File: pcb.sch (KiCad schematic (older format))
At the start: 5 parts, among them J0 USB_mini_micro_B, P1 CONN_3X2, P2 CONN_4

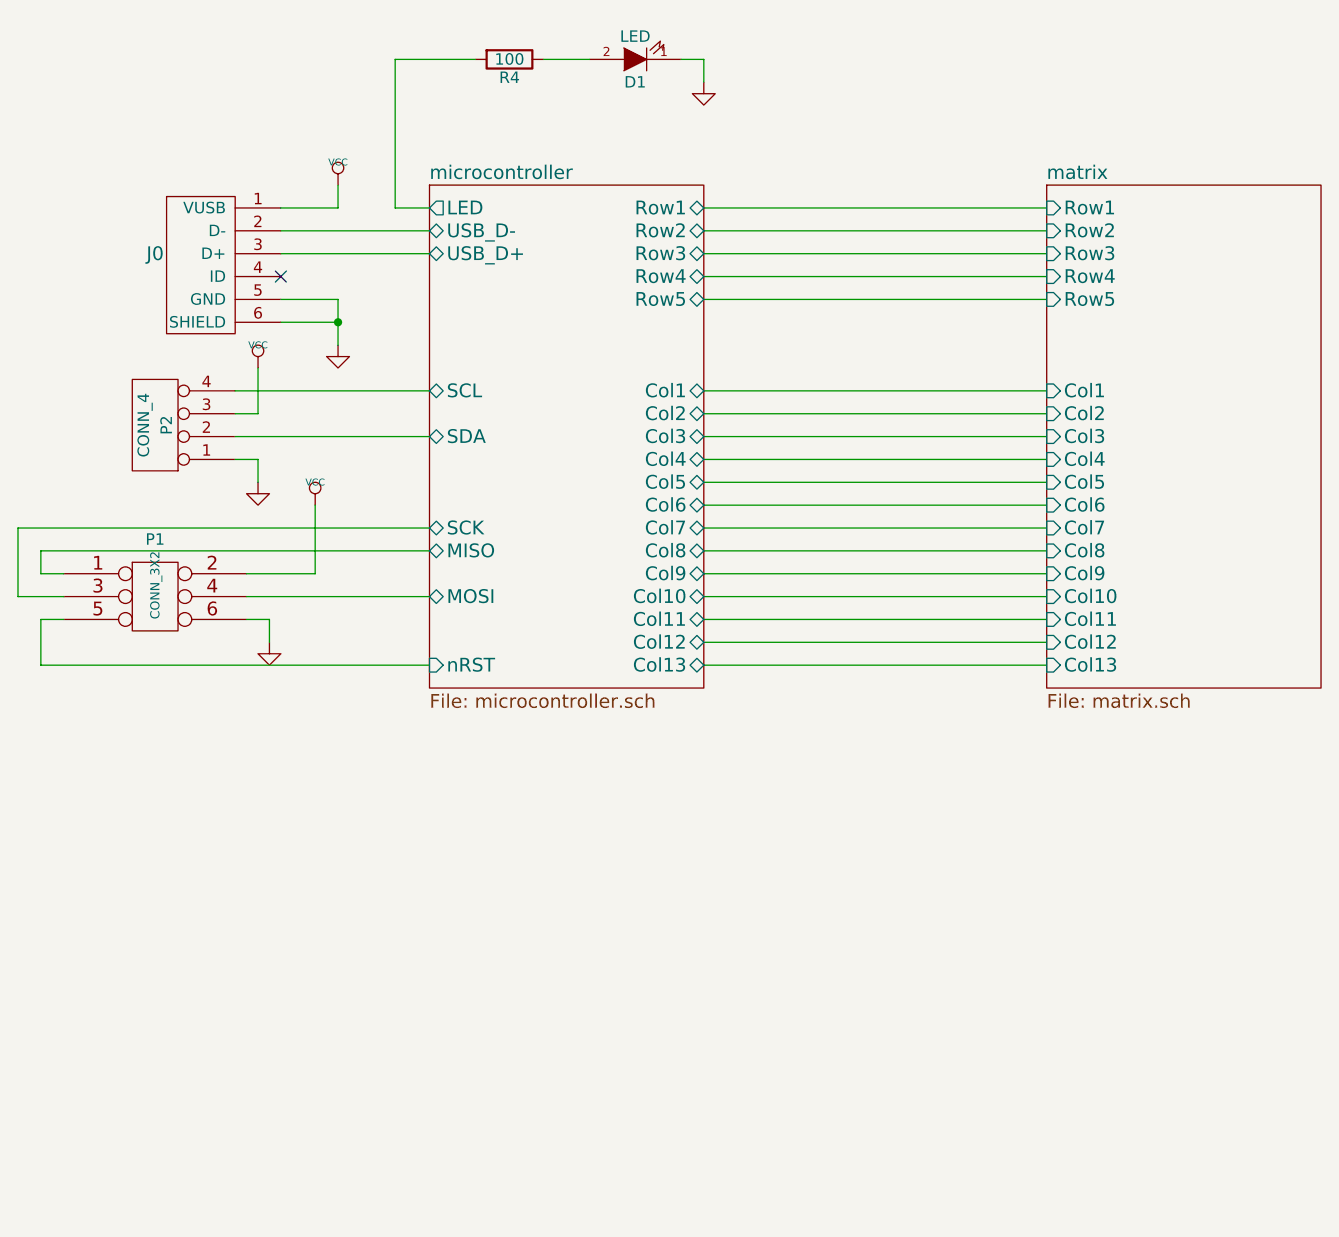
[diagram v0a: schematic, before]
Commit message: Branch for finalizing the board.
TODO:
Swap to smaller components, finalize pads
Added footprints.pretty
Add RGB underglow
Added schematic library (keenkeeb.lib/dcm)
Remove SPI header (?)
Add test pads (?)
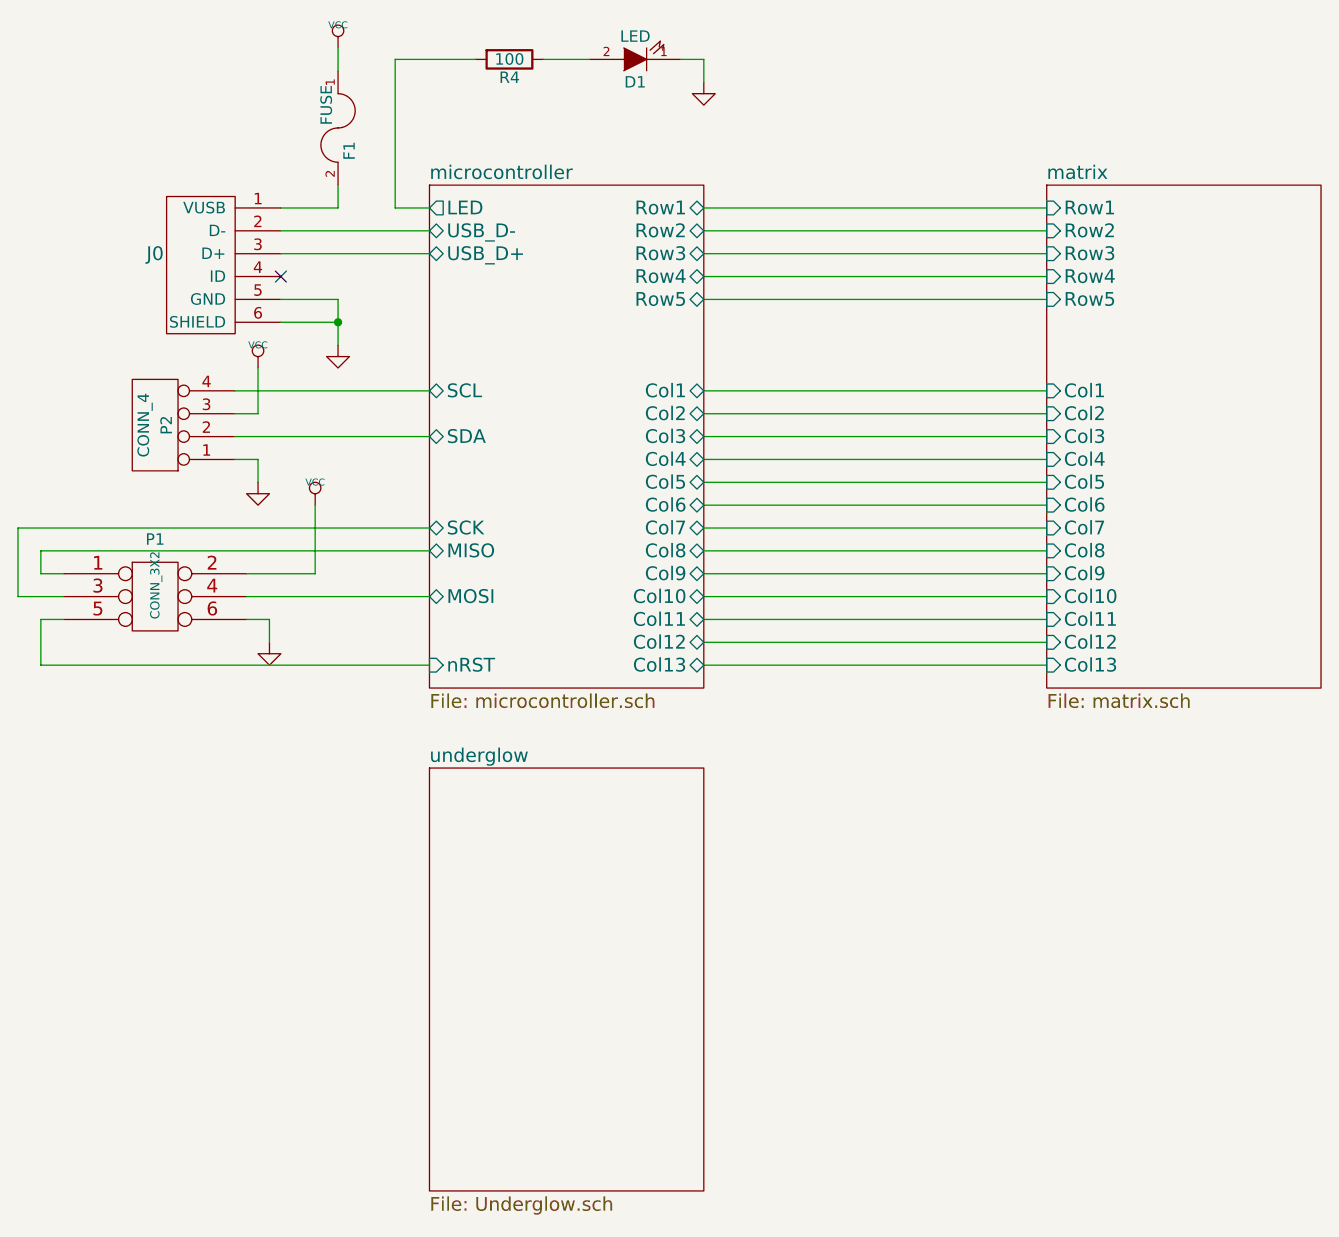
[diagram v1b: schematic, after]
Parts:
- added F1: FUSE, LEDs:LED_0805, symbol FUSE
- D1: footprint Keyboards:LED_3mm_plusminus -> footprints:LED_3mm_plusminus
- R4: footprint Resistors_SMD:R_0805_HandSoldering -> Resistors_SMD:R_0805
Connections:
- net VCC: now also F1.1; no longer J0.1 (VUSB)
- new net: F1.2, J0.1 (VUSB)
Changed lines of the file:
@@
 LIBS:contrib
 LIBS:valves
+LIBS:keenkeeb
 LIBS:keyboard_parts
 LIBS:pcb-cache
@@
 $Descr A4 11693 8268
 encoding utf-8
-Sheet 1 3
+Sheet 1 4
 Title ""
 Date ""
@@
 L VCC #PWR01
 U 1 1 587BC255
-P 3600 2250
-F 0 "#PWR01" H 3600 2350 30  0001 C CNN
-F 1 "VCC" H 3600 2350 30  0000 C CNN
-F 2 "" H 3600 2250 60  0001 C CNN
-F 3 "" H 3600 2250 60  0001 C CNN
-	1    3600 2250
+P 3600 1650
+F 0 "#PWR01" H 3600 1750 30  0001 C CNN
+F 1 "VCC" H 3600 1750 30  0000 C CNN
+F 2 "" H 3600 1650 60  0001 C CNN
+F 3 "" H 3600 1650 60  0001 C CNN
+	1    3600 1650
 	1    0    0    -1
 $EndComp
@@
 F 0 "D1" H 4900 1800 50  0000 C CNN
 F 1 "LED" H 4900 1600 50  0000 C CNN
-F 2 "Keyboards:LED_3mm_plusminus" H 4900 1700 60  0001 C CNN
+F 2 "footprints:LED_3mm_plusminus" H 4900 1700 60  0001 C CNN
 F 3 "" H 4900 1700 60  0001 C CNN
 	1    4900 1700
@@
 F 0 "R4" V 4430 1700 50  0000 C CNN
 F 1 "100" V 4350 1700 50  0000 C CNN
-F 2 "Resistors_SMD:R_0805_HandSoldering" H 4350 1700 60  0001 C CNN
+F 2 "Resistors_SMD:R_0805" H 4350 1700 60  0001 C CNN
 F 3 "" H 4350 1700 60  0001 C CNN
 	1    4350 1700
@@
 Wire Wire Line
 	5100 1700 5200 1700
+$Sheet
+S 4000 4800 1200 1850
+U 591558FE
+F0 "underglow" 60
+F1 "Underglow.sch" 60
+$EndSheet
+$Comp
+L FUSE F1
+U 1 1 5916B62D
+P 3600 2000
+F 0 "F1" H 3700 2050 50  0000 C CNN
+F 1 "FUSE" H 3500 1950 50  0000 C CNN
+F 2 "LEDs:LED_0805" H 3600 2000 50  0001 C CNN
+F 3 "" H 3600 2000 50  0000 C CNN
+	1    3600 2000
+	0    1    1    0
+$EndComp
+Wire Wire Line
+	3600 1650 3600 1750
 $EndSCHEMATC

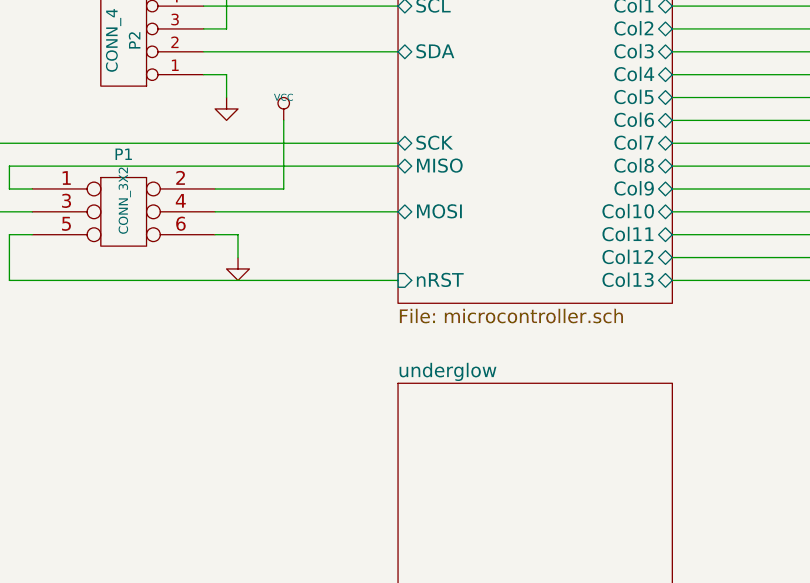
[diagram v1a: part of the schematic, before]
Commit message: ARR GEE BEE!!!
Added pads for WS2812B underglow - connected to pin 11.
Rerouted some connections.
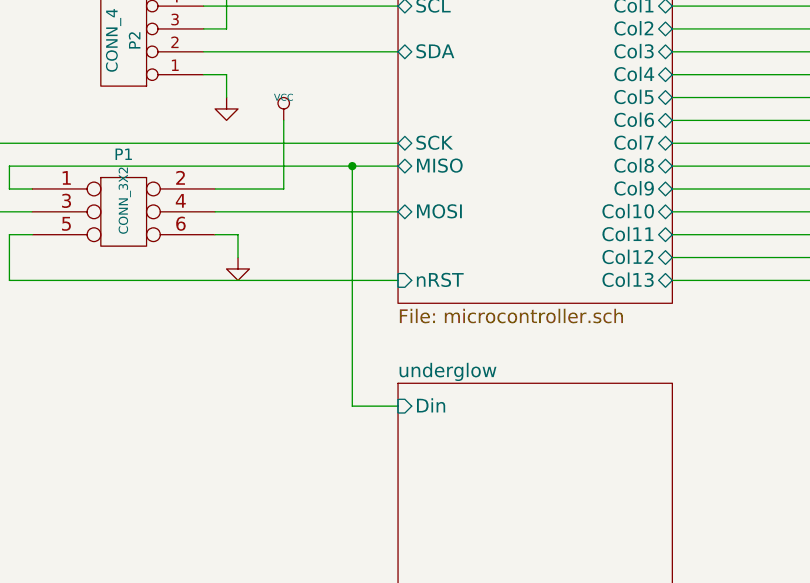
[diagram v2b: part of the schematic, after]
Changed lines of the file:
@@
 F0 "underglow" 60
 F1 "Underglow.sch" 60
+F2 "Din" I L 4000 4900 60
 $EndSheet
 $Comp
@@
 Wire Wire Line
 	3600 1650 3600 1750
+Wire Wire Line
+	4000 4900 3800 4900
+Wire Wire Line
+	3800 4900 3800 3850
+Connection ~ 3800 3850
 $EndSCHEMATC

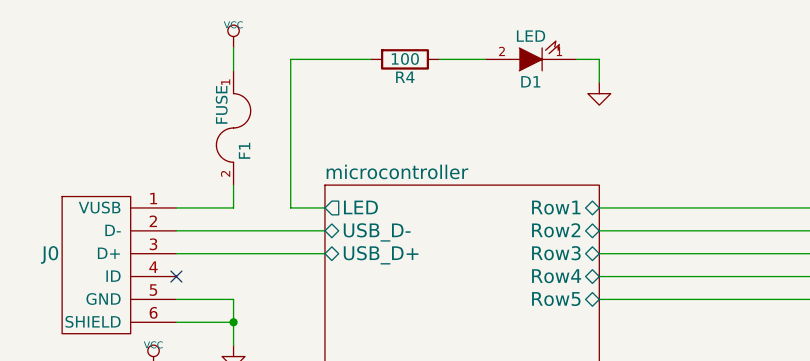
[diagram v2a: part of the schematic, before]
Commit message: Added 0.1uF caps to LEDs
Added capacitors from Vcc to GND for WS2812s
Also changed some references
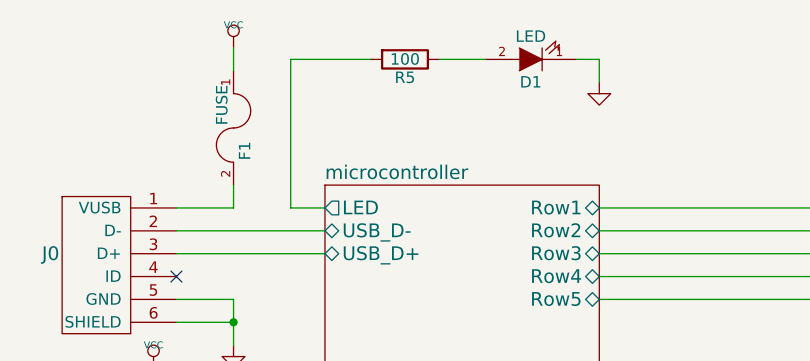
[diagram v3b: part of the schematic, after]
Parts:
- renumbered R4 to R5
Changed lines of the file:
@@
 $EndComp
 $Comp
-L R R4
+L R R5
 U 1 1 591032AE
 P 4350 1700
-F 0 "R4" V 4430 1700 50  0000 C CNN
+F 0 "R5" V 4430 1700 50  0000 C CNN
 F 1 "100" V 4350 1700 50  0000 C CNN
 F 2 "Resistors_SMD:R_0805" H 4350 1700 60  0001 C CNN

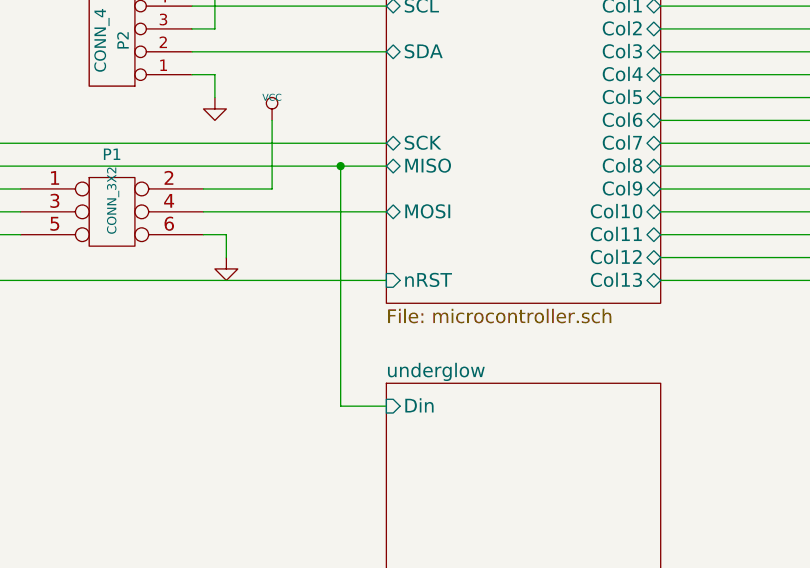
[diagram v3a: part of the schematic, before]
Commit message: Started to layout with MX/Alps footprints
Added footprints that support Cherry MX and Alps switches.
Started to layout the board with new footprints.  Will support PCB
mounted switches/stabs.
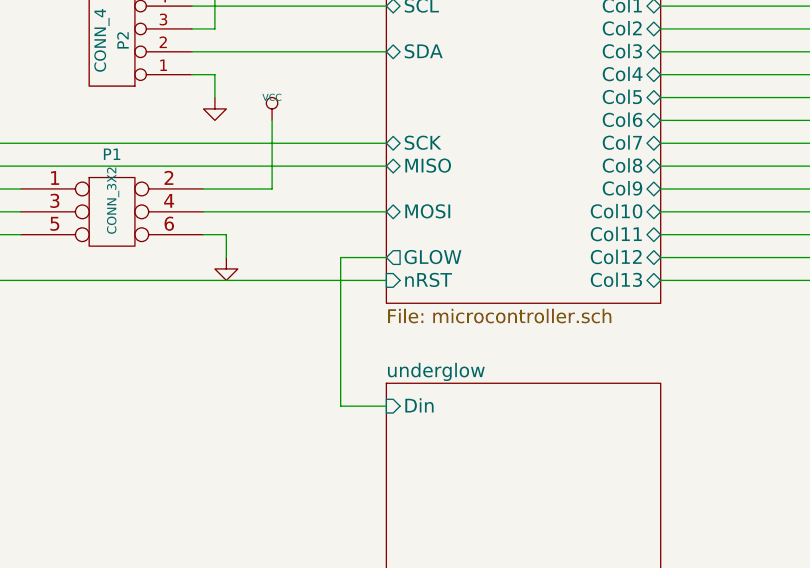
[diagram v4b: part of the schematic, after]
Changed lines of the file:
@@
 F27 "nRST" I L 4000 4350 60
 F28 "LED" O L 4000 2350 60
+F29 "GLOW" O L 4000 4250 60
 $EndSheet
 $Comp
@@
 	4000 4900 3800 4900
 Wire Wire Line
-	3800 4900 3800 3850
-Connection ~ 3800 3850
+	4000 4250 3800 4250
+Wire Wire Line
+	3800 4250 3800 4900
 $EndSCHEMATC

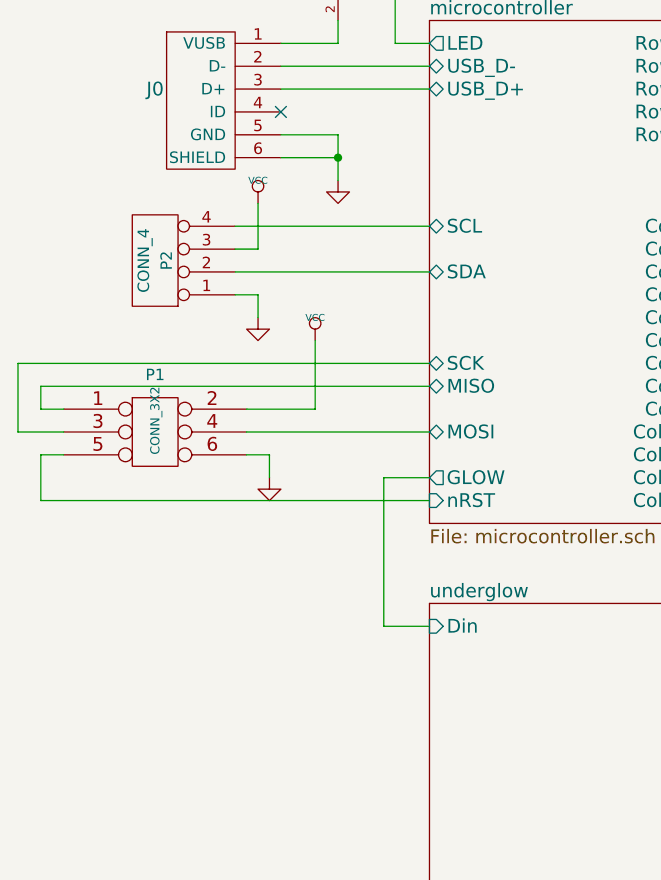
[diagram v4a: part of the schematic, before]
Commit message: Connected most of the components on the board
TODO:
Replace P1 with 1x6 header for SPI, Vcc, GND
Add test pads
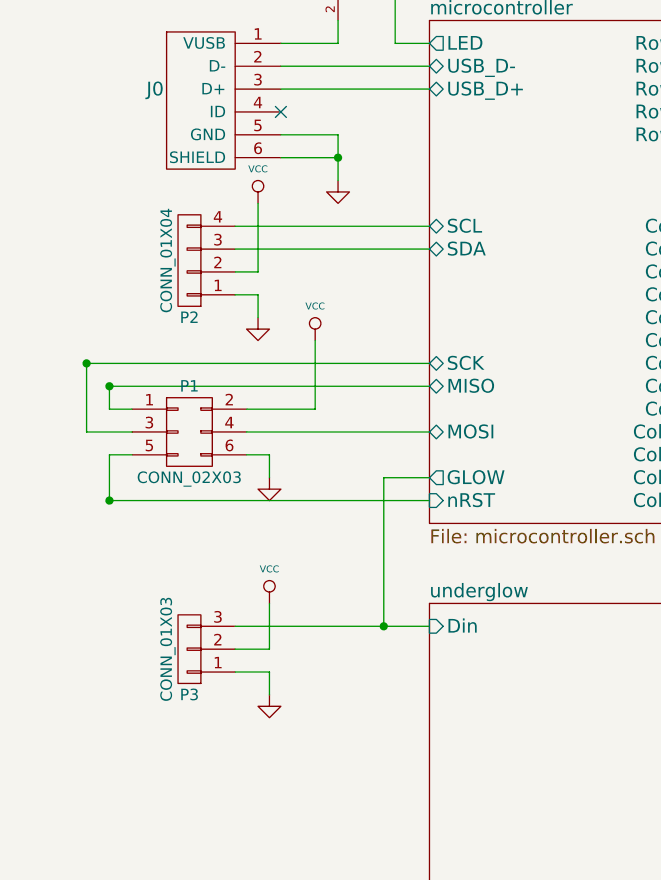
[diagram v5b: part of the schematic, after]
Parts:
- removed P1: CONN_3X2, Pin_Headers:Pin_Header_Straight_2x03_Pitch2.54mm, symbol CONN_3X2
- removed P2: CONN_4, Pin_Headers:Pin_Header_Straight_1x04_Pitch2.54mm, symbol CONN_4
- added P1: CONN_02X03, Pin_Headers:Pin_Header_Straight_2x03_Pitch2.54mm, symbol CONN_02X03
- added P2: CONN_01X04, Pin_Headers:Pin_Header_Straight_1x04_Pitch2.54mm, symbol CONN_01X04
- added P3: CONN_01X03, Pin_Headers:Pin_Header_Straight_1x03_Pitch2.54mm, symbol CONN_01X03
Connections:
- net GND: now also P1.6 (P6), P2.1 (P1), P3.1 (P1)
- net VCC: now also P1.2 (P2), P2.2 (P2), P3.2 (P2)
- net microcontroller/GLOW: now also P3.3 (P3)
- net microcontroller/MISO: now also P1.1 (P1)
- net microcontroller/MOSI: now also P1.4 (P4)
- net microcontroller/SCK: now also P1.3 (P3)
- net microcontroller/SCL: now also P2.4 (P4)
- net microcontroller/SDA: now also P2.3 (P3)
- net microcontroller/nRST: now also P1.5 (P5)
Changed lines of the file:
@@
 F21 "Row1" B R 5200 2350 60
 F22 "SCL" B L 4000 3150 60
-F23 "SDA" B L 4000 3350 60
+F23 "SDA" B L 4000 3250 60
 F24 "MISO" B L 4000 3850 60
 F25 "MOSI" B L 4000 4050 60
@@
 F29 "GLOW" O L 4000 4250 60
 $EndSheet
-$Comp
-L CONN_4 P2
-U 1 1 59085B55
-P 2800 3300
-F 0 "P2" V 2750 3300 50  0000 C CNN
-F 1 "CONN_4" V 2850 3300 50  0000 C CNN
-F 2 "Pin_Headers:Pin_Header_Straight_1x04_Pitch2.54mm" H 2800 3300 60  0001 C CNN
-F 3 "" H 2800 3300 60  0001 C CNN
-	1    2800 3300
-	-1   0    0    1
-$EndComp
 $Comp
 L GND #PWR03
@@
 P 3250 3050
 F 0 "#PWR04" H 3250 3150 30  0001 C CNN
-F 1 "VCC" H 3250 3150 30  0000 C CNN
+F 1 "VCC" H 3250 3200 30  0000 C CNN
 F 2 "" H 3250 3050 60  0001 C CNN
 F 3 "" H 3250 3050 60  0001 C CNN
 	1    3250 3050
-	1    0    0    -1
-$EndComp
-$Comp
-L CONN_3X2 P1
-U 1 1 5908D045
-P 2800 4050
-F 0 "P1" H 2800 4300 50  0000 C CNN
-F 1 "CONN_3X2" V 2800 4100 40  0000 C CNN
-F 2 "Pin_Headers:Pin_Header_Straight_2x03_Pitch2.54mm" H 2800 4050 60  0001 C CNN
-F 3 "" H 2800 4050 60  0001 C CNN
-	1    2800 4050
 	1    0    0    -1
 $EndComp
@@
 P 3500 3650
 F 0 "#PWR06" H 3500 3750 30  0001 C CNN
-F 1 "VCC" H 3500 3750 30  0000 C CNN
+F 1 "VCC" H 3500 3800 30  0000 C CNN
 F 2 "" H 3500 3650 60  0001 C CNN
 F 3 "" H 3500 3650 60  0001 C CNN
@@
 	6700 2450 5200 2450
 Wire Wire Line
-	4000 3350 3150 3350
-Wire Wire Line
 	3150 3150 4000 3150
 Wire Wire Line
@@
 	3250 3450 3250 3550
 Wire Wire Line
-	3150 3250 3250 3250
-Wire Wire Line
-	3250 3250 3250 3050
-Wire Wire Line
-	4000 3850 2300 3850
-Wire Wire Line
-	2300 3850 2300 3950
-Wire Wire Line
-	2300 3950 2400 3950
-Wire Wire Line
-	4000 3750 2200 3750
-Wire Wire Line
-	2200 3750 2200 4050
-Wire Wire Line
-	2200 4050 2400 4050
+	3250 3050 3250 3350
 Wire Wire Line
 	4000 4050 3200 4050
@@
 Wire Wire Line
 	3500 3950 3500 3650
-Wire Wire Line
-	4000 4350 2300 4350
-Wire Wire Line
-	2300 4350 2300 4150
-Wire Wire Line
-	2300 4150 2400 4150
 Wire Wire Line
 	4000 2350 3850 2350
@@
 	3600 1650 3600 1750
 Wire Wire Line
-	4000 4900 3800 4900
+	3150 4900 4000 4900
 Wire Wire Line
 	4000 4250 3800 4250
 Wire Wire Line
 	3800 4250 3800 4900
+$Comp
+L CONN_02X03 P1
+U 1 1 594B843A
+P 2950 4050
+F 0 "P1" H 2950 4250 50  0000 C CNN
+F 1 "CONN_02X03" H 2950 3850 50  0000 C CNN
+F 2 "Pin_Headers:Pin_Header_Straight_2x03_Pitch2.54mm" H 2950 2850 50  0001 C CNN
+F 3 "" H 2950 2850 50  0000 C CNN
+	1    2950 4050
+	1    0    0    -1
+$EndComp
+$Comp
+L CONN_01X04 P2
+U 1 1 594B85A5
+P 2950 3300
+F 0 "P2" H 2950 3550 50  0000 C CNN
+F 1 "CONN_01X04" V 3050 3300 50  0000 C CNN
+F 2 "Pin_Headers:Pin_Header_Straight_1x04_Pitch2.54mm" H 2950 3300 50  0001 C CNN
+F 3 "" H 2950 3300 50  0000 C CNN
+	1    2950 3300
+	-1   0    0    1
+$EndComp
+$Comp
+L CONN_01X03 P3
+U 1 1 594B8720
+P 2950 5000
+F 0 "P3" H 2950 5200 50  0000 C CNN
+F 1 "CONN_01X03" V 3050 5000 50  0000 C CNN
+F 2 "Pin_Headers:Pin_Header_Straight_1x03_Pitch2.54mm" H 2950 5000 50  0001 C CNN
+F 3 "" H 2950 5000 50  0000 C CNN
+	1    2950 5000
+	-1   0    0    1
+$EndComp
+Wire Wire Line
+	2700 3950 2600 3950
+Wire Wire Line
+	2600 3950 2600 3850
+Connection ~ 2600 3850
+Wire Wire Line
+	2700 4050 2500 4050
+Wire Wire Line
+	2500 4050 2500 3750
+Connection ~ 2500 3750
+Wire Wire Line
+	2700 4150 2600 4150
+Wire Wire Line
+	2600 4150 2600 4350
+Connection ~ 2600 4350
+Wire Wire Line
+	2600 4350 4000 4350
+Wire Wire Line
+	2500 3750 4000 3750
+Wire Wire Line
+	2600 3850 4000 3850
+Connection ~ 3800 4900
+Wire Wire Line
+	3150 5000 3300 5000
+Wire Wire Line
+	3300 5000 3300 4800
+Wire Wire Line
+	3150 5100 3300 5100
+Wire Wire Line
+	3300 5100 3300 5200
+$Comp
+L GND #PWR08
+U 1 1 594BD05A
+P 3300 5200
+F 0 "#PWR08" H 3300 5200 30  0001 C CNN
+F 1 "GND" H 3300 5130 30  0001 C CNN
+F 2 "" H 3300 5200 60  0001 C CNN
+F 3 "" H 3300 5200 60  0001 C CNN
+	1    3300 5200
+	1    0    0    -1
+$EndComp
+$Comp
+L VCC #PWR09
+U 1 1 594BD194
+P 3300 4800
+F 0 "#PWR09" H 3300 4900 30  0001 C CNN
+F 1 "VCC" H 3300 4950 30  0000 C CNN
+F 2 "" H 3300 4800 60  0001 C CNN
+F 3 "" H 3300 4800 60  0001 C CNN
+	1    3300 4800
+	1    0    0    -1
+$EndComp
+Wire Wire Line
+	3250 3350 3150 3350
+Wire Wire Line
+	3150 3250 4000 3250
 $EndSCHEMATC
